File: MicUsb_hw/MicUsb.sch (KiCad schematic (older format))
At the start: 80 parts, among them Q1 DVIUC6-4SC6, SW1 BUTTON

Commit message: * filter once more
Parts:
- gave numbers to parts that had none: 17
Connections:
- net ADC_IN: now also C32.1, DA4.13 (-), DA4.14; no longer F6.1, R5.3
- net AMP_OUT: now reaches R12.2
- net AMP_OUT: now also F6.1, R5.3
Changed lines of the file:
@@
 	-1   0    0    -1
 $EndComp
-Text Label 7000 3350 2    60   ~ 0
+Text Label 15800 5300 2    60   ~ 0
 ADC_IN
 $Comp
@@
 $EndComp
 $Comp
-L Generic_14pin DA?
+L Generic_14pin DA4
 U 1 1 56533834
 P 7700 5300
-F 0 "DA?" H 7750 5500 60  0000 C CNN
+F 0 "DA4" H 7750 5500 60  0000 C CNN
 F 1 "Generic_14pin" H 7900 5100 50  0000 C CNN
 F 2 "" H 7700 5300 60  0000 C CNN
@@
 $EndComp
 $Comp
-L R R?
+L R R13
 U 1 1 56533B0F
 P 6750 5200
-F 0 "R?" V 6830 5050 50  0000 C CNN
+F 0 "R13" V 6830 5050 50  0000 C CNN
 F 1 "75k" V 6750 5200 50  0000 C CNN
 F 2 "RES_0603" V 6830 5300 28  0000 C CNN
@@
 $EndComp
 $Comp
-L R R?
+L R R12
 U 1 1 56533BBE
 P 6150 5200
-F 0 "R?" V 6230 5050 50  0000 C CNN
+F 0 "R12" V 6230 5050 50  0000 C CNN
 F 1 "39k" V 6150 5200 50  0000 C CNN
 F 2 "RES_0603" V 6230 5300 28  0000 C CNN
@@
 $EndComp
 $Comp
-L AGND #PWR?
+L AGND #PWR076
 U 1 1 56534E8F
 P 7600 5750
-F 0 "#PWR?" H 7600 5750 40  0001 C CNN
+F 0 "#PWR076" H 7600 5750 40  0001 C CNN
 F 1 "AGND" H 7600 5680 50  0001 C CNN
 F 2 "" H 7600 5750 60  0000 C CNN
@@
 	8200 5300 8100 5300
 $Comp
-L C C?
+L C C27
 U 1 1 5653519E
 P 7100 5500
-F 0 "C?" H 7000 5400 50  0000 L CNN
+F 0 "C27" H 7000 5400 50  0000 L CNN
 F 1 "1n" H 7000 5600 50  0000 L CNN
 F 2 "CAP_0603" V 7200 5350 28  0000 C BNN
@@
 	6400 5200 6500 5200
 $Comp
-L AGND #PWR?
+L AGND #PWR077
 U 1 1 56535776
 P 7100 5750
-F 0 "#PWR?" H 7100 5750 40  0001 C CNN
+F 0 "#PWR077" H 7100 5750 40  0001 C CNN
 F 1 "AGND" H 7100 5680 50  0001 C CNN
 F 2 "" H 7100 5750 60  0000 C CNN
@@
 Connection ~ 8200 5300
 $Comp
-L +3.3V_A #PWR?
+L +3.3V_A #PWR078
 U 1 1 56535A75
 P 7600 4800
-F 0 "#PWR?" H 7600 4760 30  0001 C CNN
+F 0 "#PWR078" H 7600 4760 30  0001 C CNN
 F 1 "+3.3V_A" H 7680 4830 30  0000 C CNN
 F 2 "" H 7600 4800 60  0000 C CNN
@@
 	7600 4950 7600 4800
 $Comp
-L C C?
+L C C26
 U 1 1 56538884
 P 6950 4600
-F 0 "C?" V 6900 4450 50  0000 L CNN
+F 0 "C26" V 6900 4450 50  0000 L CNN
 F 1 "2.2n" V 6900 4650 50  0000 L CNN
 F 2 "CAP_0603" V 7050 4450 28  0000 C BNN
@@
 	7100 5750 7100 5700
 $Comp
-L Generic_14pin DA?
+L Generic_14pin DA4
 U 2 1 5653AAF6
 P 10100 5300
-F 0 "DA?" H 10150 5500 60  0000 C CNN
+F 0 "DA4" H 10150 5500 60  0000 C CNN
 F 1 "Generic_14pin" H 10300 5100 50  0000 C CNN
 F 2 "" H 10100 5300 60  0000 C CNN
@@
 $EndComp
 $Comp
-L R R?
+L R R14
 U 1 1 5653ABDD
 P 8550 5200
-F 0 "R?" V 8630 5050 50  0000 C CNN
+F 0 "R14" V 8630 5050 50  0000 C CNN
 F 1 "9.1k" V 8550 5200 50  0000 C CNN
 F 2 "RES_0603" V 8630 5300 28  0000 C CNN
@@
 $EndComp
 $Comp
-L R R?
+L R R15
 U 1 1 5653ADD6
 P 9150 5200
-F 0 "R?" V 9230 5050 50  0000 C CNN
+F 0 "R15" V 9230 5050 50  0000 C CNN
 F 1 "15k" V 9150 5200 50  0000 C CNN
 F 2 "RES_0603" V 9230 5300 28  0000 C CNN
@@
 	9400 5200 9700 5200
 $Comp
-L C C?
+L C C29
 U 1 1 5653B544
 P 9500 5500
-F 0 "C?" H 9400 5400 50  0000 L CNN
+F 0 "C29" H 9400 5400 50  0000 L CNN
 F 1 "1n" H 9400 5600 50  0000 L CNN
 F 2 "CAP_0603" V 9600 5350 28  0000 C BNN
@@
 $EndComp
 $Comp
-L AGND #PWR?
+L AGND #PWR079
 U 1 1 5653B5E5
 P 9500 5750
-F 0 "#PWR?" H 9500 5750 40  0001 C CNN
+F 0 "#PWR079" H 9500 5750 40  0001 C CNN
 F 1 "AGND" H 9500 5680 50  0001 C CNN
 F 2 "" H 9500 5750 60  0000 C CNN
@@
 $EndComp
 $Comp
-L AGND #PWR?
+L AGND #PWR080
 U 1 1 5653B683
 P 10000 5750
-F 0 "#PWR?" H 10000 5750 40  0001 C CNN
+F 0 "#PWR080" H 10000 5750 40  0001 C CNN
 F 1 "AGND" H 10000 5680 50  0001 C CNN
 F 2 "" H 10000 5750 60  0000 C CNN
@@
 $EndComp
 $Comp
-L +3.3V_A #PWR?
+L +3.3V_A #PWR081
 U 1 1 5653B721
 P 10000 4800
-F 0 "#PWR?" H 10000 4760 30  0001 C CNN
+F 0 "#PWR081" H 10000 4760 30  0001 C CNN
 F 1 "+3.3V_A" H 10080 4830 30  0000 C CNN
 F 2 "" H 10000 4800 60  0000 C CNN
@@
 	10000 4950 10000 4800
 $Comp
-L C C?
+L C C28
 U 1 1 5653BE69
 P 9350 4600
-F 0 "C?" V 9300 4450 50  0000 L CNN
+F 0 "C28" V 9300 4450 50  0000 L CNN
 F 1 "12n" V 9300 4650 50  0000 L CNN
 F 2 "CAP_0603" V 9450 4450 28  0000 C BNN
@@
 Connection ~ 8850 5200
 $Comp
-L Generic_14pin DA?
+L Generic_14pin DA4
 U 3 1 5653E042
 P 12500 5300
-F 0 "DA?" H 12550 5500 60  0000 C CNN
+F 0 "DA4" H 12550 5500 60  0000 C CNN
 F 1 "Generic_14pin" H 12700 5100 50  0000 C CNN
 F 2 "" H 12500 5300 60  0000 C CNN
@@
 $EndComp
 $Comp
-L R R?
+L R R16
 U 1 1 5653E12D
 P 10950 5200
-F 0 "R?" V 11030 5050 50  0000 C CNN
+F 0 "R16" V 11030 5050 50  0000 C CNN
 F 1 "3k" V 10950 5200 50  0000 C CNN
 F 2 "RES_0603" V 11030 5300 28  0000 C CNN
@@
 $EndComp
 $Comp
-L R R?
+L R R17
 U 1 1 5653E226
 P 11550 5200
-F 0 "R?" V 11630 5050 50  0000 C CNN
+F 0 "R17" V 11630 5050 50  0000 C CNN
 F 1 "3k" V 11550 5200 50  0000 C CNN
 F 2 "RES_0603" V 11630 5300 28  0000 C CNN
@@
 $EndComp
 $Comp
-L C C?
+L C C31
 U 1 1 5653E3CC
 P 11900 5500
-F 0 "C?" H 11800 5400 50  0000 L CNN
+F 0 "C31" H 11800 5400 50  0000 L CNN
 F 1 "2.2n" H 11800 5600 50  0000 L CNN
 F 2 "CAP_0603" V 12000 5350 28  0000 C BNN
@@
 $EndComp
 $Comp
-L AGND #PWR?
+L AGND #PWR082
 U 1 1 5653E47F
 P 11900 5750
-F 0 "#PWR?" H 11900 5750 40  0001 C CNN
+F 0 "#PWR082" H 11900 5750 40  0001 C CNN
 F 1 "AGND" H 11900 5680 50  0001 C CNN
 F 2 "" H 11900 5750 60  0000 C CNN
@@
 $EndComp
 $Comp
-L AGND #PWR?
+L AGND #PWR083
 U 1 1 5653E527
 P 12400 5750
-F 0 "#PWR?" H 12400 5750 40  0001 C CNN
+F 0 "#PWR083" H 12400 5750 40  0001 C CNN
 F 1 "AGND" H 12400 5680 50  0001 C CNN
 F 2 "" H 12400 5750 60  0000 C CNN
@@
 $EndComp
 $Comp
-L +3.3V_A #PWR?
+L +3.3V_A #PWR084
 U 1 1 5653E5CF
 P 12400 4800
-F 0 "#PWR?" H 12400 4760 30  0001 C CNN
+F 0 "#PWR084" H 12400 4760 30  0001 C CNN
 F 1 "+3.3V_A" H 12480 4830 30  0000 C CNN
 F 2 "" H 12400 4800 60  0000 C CNN
@@
 $EndComp
 $Comp
-L C C?
+L C C30
 U 1 1 5653E677
 P 11750 4600
-F 0 "C?" V 11700 4450 50  0000 L CNN
+F 0 "C30" V 11700 4450 50  0000 L CNN
 F 1 "47n" V 11700 4650 50  0000 L CNN
 F 2 "CAP_0603" V 11850 4450 28  0000 C BNN
@@
 Connection ~ 11250 5200
 $Comp
-L Generic_14pin DA?
+L Generic_14pin DA4
 U 4 1 56540686
 P 14900 5300
-F 0 "DA?" H 14950 5500 60  0000 C CNN
+F 0 "DA4" H 14950 5500 60  0000 C CNN
 F 1 "Generic_14pin" H 15100 5100 50  0000 C CNN
 F 2 "" H 14900 5300 60  0000 C CNN
@@
 $EndComp
 $Comp
-L R R?
+L R R18
 U 1 1 5654068C
 P 13350 5200
-F 0 "R?" V 13430 5050 50  0000 C CNN
+F 0 "R18" V 13430 5050 50  0000 C CNN
 F 1 "69.8R" V 13350 5200 50  0000 C CNN
 F 2 "RES_0603" V 13430 5300 28  0000 C CNN
@@
 $EndComp
 $Comp
-L R R?
+L R R19
 U 1 1 56540692
 P 13950 5200
-F 0 "R?" V 14030 5050 50  0000 C CNN
+F 0 "R19" V 14030 5050 50  0000 C CNN
 F 1 "130R" V 13950 5200 50  0000 C CNN
 F 2 "RES_0603" V 14030 5300 28  0000 C CNN
@@
 $EndComp
 $Comp
-L C C?
+L C C33
 U 1 1 56540698
 P 14300 5500
-F 0 "C?" H 14200 5400 50  0000 L CNN
+F 0 "C33" H 14200 5400 50  0000 L CNN
 F 1 "15n" H 14200 5600 50  0000 L CNN
 F 2 "CAP_0603" V 14400 5350 28  0000 C BNN
@@
 $EndComp
 $Comp
-L AGND #PWR?
+L AGND #PWR085
 U 1 1 5654069E
 P 14300 5750
-F 0 "#PWR?" H 14300 5750 40  0001 C CNN
+F 0 "#PWR085" H 14300 5750 40  0001 C CNN
 F 1 "AGND" H 14300 5680 50  0001 C CNN
 F 2 "" H 14300 5750 60  0000 C CNN
@@
 $EndComp
 $Comp
-L AGND #PWR?
+L AGND #PWR086
 U 1 1 565406A4
 P 14800 5750
-F 0 "#PWR?" H 14800 5750 40  0001 C CNN
+F 0 "#PWR086" H 14800 5750 40  0001 C CNN
 F 1 "AGND" H 14800 5680 50  0001 C CNN
 F 2 "" H 14800 5750 60  0000 C CNN
@@
 $EndComp
 $Comp
-L +3.3V_A #PWR?
+L +3.3V_A #PWR087
 U 1 1 565406AA
 P 14800 4800
-F 0 "#PWR?" H 14800 4760 30  0001 C CNN
+F 0 "#PWR087" H 14800 4760 30  0001 C CNN
 F 1 "+3.3V_A" H 14880 4830 30  0000 C CNN
 F 2 "" H 14800 4800 60  0000 C CNN
@@
 $EndComp
 $Comp
-L C C?
+L C C32
 U 1 1 565406B0
 P 14150 4600
-F 0 "C?" V 14100 4450 50  0000 L CNN
+F 0 "C32" V 14100 4450 50  0000 L CNN
 F 1 "4.7u" V 14100 4650 50  0000 L CNN
 F 2 "CAP_0603" V 14250 4450 28  0000 C BNN
@@
 Wire Wire Line
 	5900 5200 5550 5200
+Text Label 5550 5200 0    60   ~ 0
+AMP_OUT
+Text Label 7000 3350 2    60   ~ 0
+AMP_OUT
 $EndSCHEMATC

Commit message: small scheme update
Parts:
- C26, C27, C28, C29, C30, C31, C32, C33: footprint CAP_0603 -> Capacitors:CAP_0603
- DA4: value Generic_14pin -> LMV324
- R12, R13, R14, R15, R16, R17, R18, R19: footprint RES_0603 -> Resistors:RES_0603
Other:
- moved on the sheet: C11, C18, C22, C23, C26, C27, C28, C29, C30, C31, C32, C33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

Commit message: just CvPcb
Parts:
- DA4: footprint (none) -> SO_DIL_TSSOP:SO14
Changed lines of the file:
@@
 L GND #PWR013
 U 1 1 564BB9D5
-P 11250 10000
-F 0 "#PWR013" H 11340 9980 30  0001 C CNN
-F 1 "GND" H 11250 9920 30  0001 C CNN
-F 2 "" H 11250 10000 60  0000 C CNN
-F 3 "" H 11250 10000 60  0000 C CNN
-	1    11250 10000
+P 11350 10000
+F 0 "#PWR013" H 11440 9980 30  0001 C CNN
+F 1 "GND" H 11350 9920 30  0001 C CNN
+F 2 "" H 11350 10000 60  0000 C CNN
+F 3 "" H 11350 10000 60  0000 C CNN
+	1    11350 10000
 	1    0    0    -1
 $EndComp
@@
 	7800 10000 7800 9750
 Wire Wire Line
-	11250 9550 11250 10000
-Wire Wire Line
 	11150 9550 11150 9750
 Wire Wire Line
-	10950 9750 11600 9750
-Connection ~ 11250 9750
-Wire Wire Line
-	11350 9750 11350 9550
-Wire Wire Line
-	10950 9550 10950 9750
-Connection ~ 11150 9750
+	11150 9750 11600 9750
+Wire Wire Line
+	11350 9550 11350 10000
 Wire Wire Line
 	11450 9750 11450 9550
@@
 F 0 "DA4" H 5350 2150 60  0000 C CNN
 F 1 "LMV324" H 5400 1750 50  0000 C CNN
-F 2 "" H 5300 1950 60  0001 C CNN
+F 2 "SO_DIL_TSSOP:SO14" H 5300 1950 60  0001 C CNN
 F 3 "" H 5300 1950 60  0000 C CNN
 	1    5300 1950
@@
 F 0 "DA4" H 7750 2150 60  0000 C CNN
 F 1 "LMV324" H 7800 1750 50  0000 C CNN
-F 2 "" H 7700 1950 60  0001 C CNN
+F 2 "SO_DIL_TSSOP:SO14" H 7700 1950 60  0001 C CNN
 F 3 "" H 7700 1950 60  0000 C CNN
 	2    7700 1950
@@
 F 0 "DA4" H 10150 2150 60  0000 C CNN
 F 1 "LMV324" H 10200 1750 50  0000 C CNN
-F 2 "" H 10100 1950 60  0001 C CNN
+F 2 "SO_DIL_TSSOP:SO14" H 10100 1950 60  0001 C CNN
 F 3 "" H 10100 1950 60  0000 C CNN
 	3    10100 1950
@@
 F 0 "DA4" H 12550 2150 60  0000 C CNN
 F 1 "LMV324" H 12600 1750 50  0000 C CNN
-F 2 "" H 12500 1950 60  0001 C CNN
+F 2 "SO_DIL_TSSOP:SO14" H 12500 1950 60  0001 C CNN
 F 3 "" H 12500 1950 60  0000 C CNN
 	4    12500 1950
@@
 Text Label 6900 5750 2    60   ~ 0
 AMP_OUT
+Wire Wire Line
+	11250 9550 11250 9750
+Connection ~ 11250 9750
 $EndSCHEMATC

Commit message: * pcb 50%
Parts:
- added TP1, TP2, TP3: TESTPOINT, PCB:TESTPOINT_1MM, symbol TESTPOINT
- D2, D3, D4, D5: footprint LEDs:LED_0603 -> LEDs:LED_Through-Hole-3mm
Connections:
- net CSIN: now also TP1.1
- net DOUT: now also TP3.1
- net SCK: now also TP2.1
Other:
- note added: "ADC\n"
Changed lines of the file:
@@
 F 0 "D2" H 8400 7140 50  0000 C CNN
 F 1 "LED" H 8220 7140 50  0000 C CNN
-F 2 "LEDs:LED_0603" H 8300 7000 60  0001 C CNN
+F 2 "LEDs:LED_Through-Hole-3mm" H 8300 7000 60  0001 C CNN
 F 3 "" H 8300 7000 60  0000 C CNN
 	1    8300 7000
@@
 F 0 "D3" H 8400 6550 50  0000 C CNN
 F 1 "LED" H 8200 6550 50  0000 C CNN
-F 2 "LEDs:LED_0603" H 8300 6700 60  0001 C CNN
+F 2 "LEDs:LED_Through-Hole-3mm" H 8300 6700 60  0001 C CNN
 F 3 "" H 8300 6700 60  0000 C CNN
 	1    8300 6700
@@
 F 0 "D4" H 8400 7440 50  0000 C CNN
 F 1 "LED" H 8220 7440 50  0000 C CNN
-F 2 "LEDs:LED_0603" H 8300 7300 60  0001 C CNN
+F 2 "LEDs:LED_Through-Hole-3mm" H 8300 7300 60  0001 C CNN
 F 3 "" H 8300 7300 60  0000 C CNN
 	1    8300 7300
@@
 F 0 "D5" H 8400 7740 50  0000 C CNN
 F 1 "LED" H 8220 7740 50  0000 C CNN
-F 2 "LEDs:LED_0603" H 8300 7600 60  0001 C CNN
+F 2 "LEDs:LED_Through-Hole-3mm" H 8300 7600 60  0001 C CNN
 F 3 "" H 8300 7600 60  0000 C CNN
 	1    8300 7600
@@
 	14350 4950 14350 5050
 Wire Wire Line
-	12950 7400 13300 7400
+	12950 7400 13350 7400
 Wire Wire Line
 	13600 3950 13900 3950
 Wire Wire Line
-	12950 7300 13300 7300
+	12950 7300 13350 7300
 Wire Wire Line
 	13600 4150 13900 4150
 Wire Wire Line
-	12950 7500 13300 7500
+	12950 7500 13350 7500
 Wire Wire Line
 	13900 4050 13600 4050
@@
 	11250 9550 11250 9750
 Connection ~ 11250 9750
+Text Notes 13050 3550 0    60   ~ 0
+ADC\n
+$Comp
+L TESTPOINT TP1
+U 1 1 5656E9F6
+P 13350 7300
+F 0 "TP1" V 13300 7500 60  0000 C CNN
+F 1 "TESTPOINT" H 13325 7525 60  0001 C CNN
+F 2 "PCB:TESTPOINT_1MM" H 13350 7300 60  0001 C CNN
+F 3 "" H 13350 7300 60  0000 C CNN
+	1    13350 7300
+	0    1    1    0
+$EndComp
+$Comp
+L TESTPOINT TP2
+U 1 1 5656EADF
+P 13350 7400
+F 0 "TP2" V 13350 7600 60  0000 C CNN
+F 1 "TESTPOINT" H 13325 7625 60  0001 C CNN
+F 2 "PCB:TESTPOINT_1MM" H 13350 7400 60  0001 C CNN
+F 3 "" H 13350 7400 60  0000 C CNN
+	1    13350 7400
+	0    1    1    0
+$EndComp
+$Comp
+L TESTPOINT TP3
+U 1 1 5656EBA0
+P 13350 7500
+F 0 "TP3" V 13400 7700 60  0000 C CNN
+F 1 "TESTPOINT" H 13325 7725 60  0001 C CNN
+F 2 "PCB:TESTPOINT_1MM" H 13350 7500 60  0001 C CNN
+F 3 "" H 13350 7500 60  0000 C CNN
+	1    13350 7500
+	0    1    1    0
+$EndComp
 $EndSCHEMATC

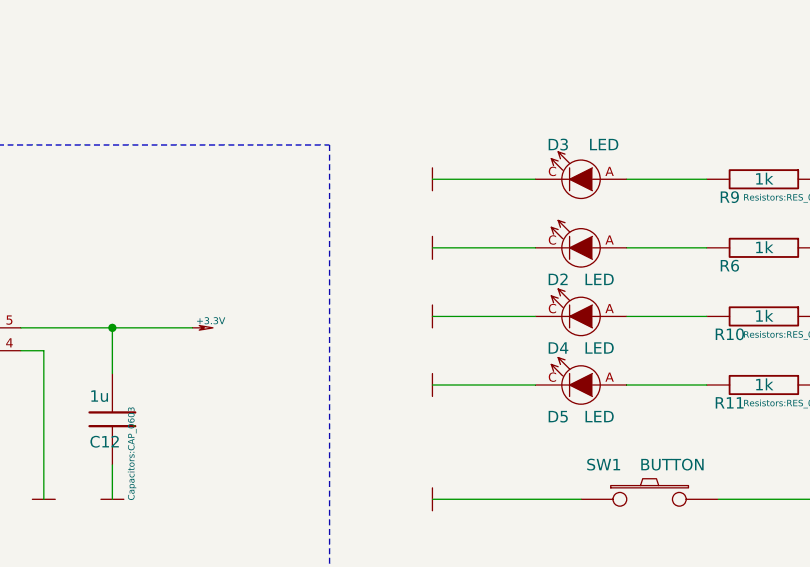
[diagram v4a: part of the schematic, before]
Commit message: * Leds renamed + Kl_lib fast pin setup + Button regulated gain + Sch leds renamed
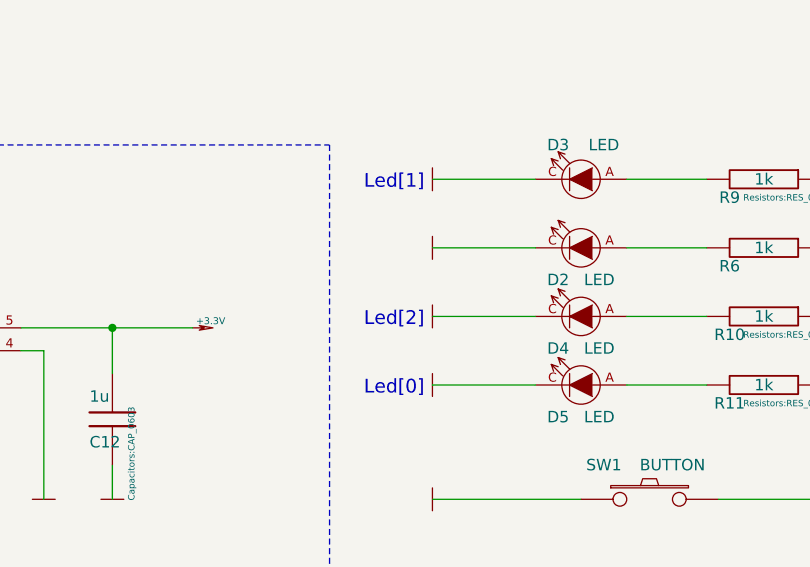
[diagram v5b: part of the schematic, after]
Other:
- note added: "Led[0]"
- note added: "Led[1]"
- note added: "Led[2]"
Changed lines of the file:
@@
 	0    1    1    0
 $EndComp
+Text Notes 7350 7650 0    60   ~ 0
+Led[0]
+Text Notes 7350 6750 0    60   ~ 0
+Led[1]
+Text Notes 7350 7350 0    60   ~ 0
+Led[2]
 $EndSCHEMATC
